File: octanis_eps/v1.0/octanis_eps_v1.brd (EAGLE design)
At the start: 80 x 50 mm, 156 parts, among them Q1 CSD16327Q3_DQG_8, Q2 CSD16327Q3_DQG_8, Q3 CSD16327Q3_DQG_8, Q4 BSS123, Q5 CSD16327Q3_DQG_8, Q6 CSD16327Q3_DQG_8, Q7 BSC0901NS, U1 MSP430FR5969, U10 INA213, U11 MIC5019, U12 TPS61088, U2 OPA2333DGK, U3 TPS2022D, U4 TPS630250YFFT, U5 BQ24650_RVA_16, U6 TPS630250YFFT, U7 TPS61232, U8 TPS630250YFFT, U9 INA213, X1 32.768kHz

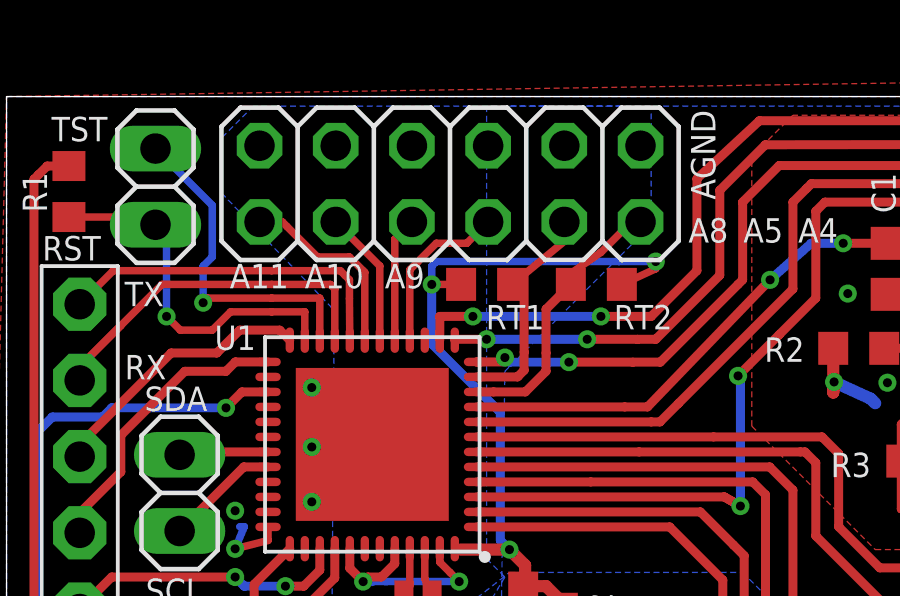
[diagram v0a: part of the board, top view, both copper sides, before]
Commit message: adjusted final resistor values for eps v1.0
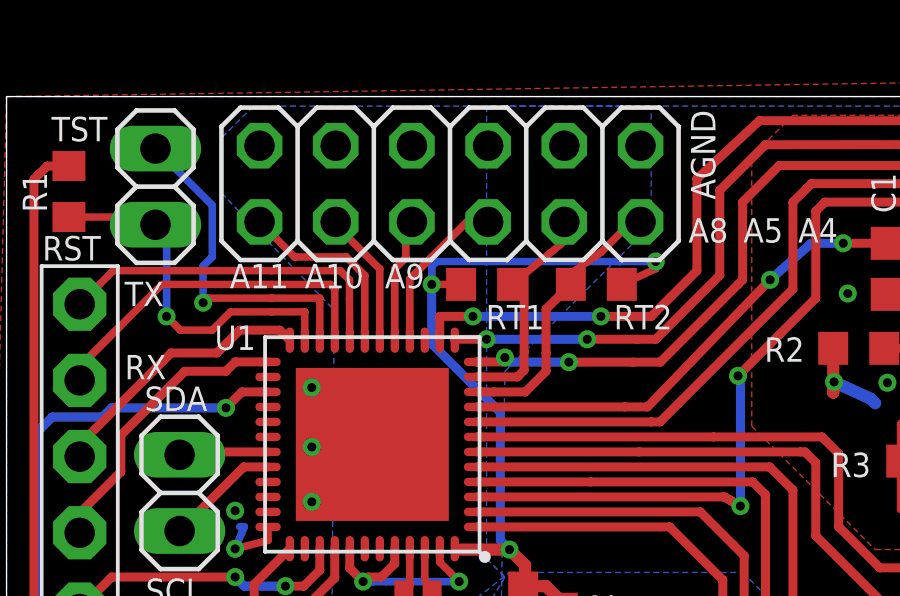
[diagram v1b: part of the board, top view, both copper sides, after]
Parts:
- C28: value 1u -> 1uF
- R2, R23: value 200k -> 200k (0.1%)
- R25, R9: value 200k -> 330k (0.1%)
- R28: value 1M -> dnp
- R29: value (none) -> Rmpph
- R3, R4, R6, R8: value 100k -> 100k (0.1%)
- R33: value (none) -> Rmppl
- R34, R35: value 100k -> 100k (1%)
- R41: value 2.2M -> 2.2M (1%)
- R47: value 470k -> 456k
- RS2, RS3: value 50m -> 10m
- RT3: value 2723 -> 2696
- RT4: value 8501 -> 8187
- RTH: value (none) -> 103AT
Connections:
- net A4_EXT renamed A_EXT0
- removed net A5_EXT: JP2.9, RT1.2, U1.11
- new net A_EXT5: JP2.1, U1.19
- net A_EXT1: now also JP2.9, RT1.2, U1.11; no longer JP2.7, U1.16
- net A_EXT2: now also JP2.7, U1.16; no longer JP2.5, U1.17
- net A_EXT3: now also JP2.5, U1.17; no longer JP2.3, U1.18
- net A_EXT4: now also JP2.3, U1.18; no longer JP2.1, U1.19
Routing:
- net A5_EXT: track 7.78 -> 0.00 mm
- net A_EXT5: track 0.00 -> 6.41 mm
- net A_EXT1: track 5.62 -> 7.78 mm
- net A_EXT4: track 6.47 -> 4.55 mm
- net A_EXT2: track 4.18 -> 5.44 mm

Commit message: EPS v2.0 finished routing
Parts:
- R44: value 100k -> 100k (1%)
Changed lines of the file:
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@@
 <attribute name="VALUE" x="60.0282" y="3.2766" size="1.27" layer="27" rot="R270"/>
 </element>
-<element name="R44" library="resistor" package="R0603" value="100k" x="64.9732" y="12.8016" smashed="yes" rot="R270">
+<element name="R44" library="resistor" package="R0603" value="100k (1%)" x="64.9732" y="12.8016" smashed="yes" rot="R270">
 <attribute name="NAME" x="65.3542" y="14.4846" size="0.8128" layer="25" rot="R90"/>
 <attribute name="VALUE" x="63.0682" y="13.4366" size="1.27" layer="27" rot="R270"/>
